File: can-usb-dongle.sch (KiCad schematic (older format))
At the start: 32 parts, among them P1 USB_A, SW1 SW_PUSH, U1 STM32F302C8T, U2 SN65HVD256, U3 MCP1700, U4 SiP32431, X1 8MHz 10ppm

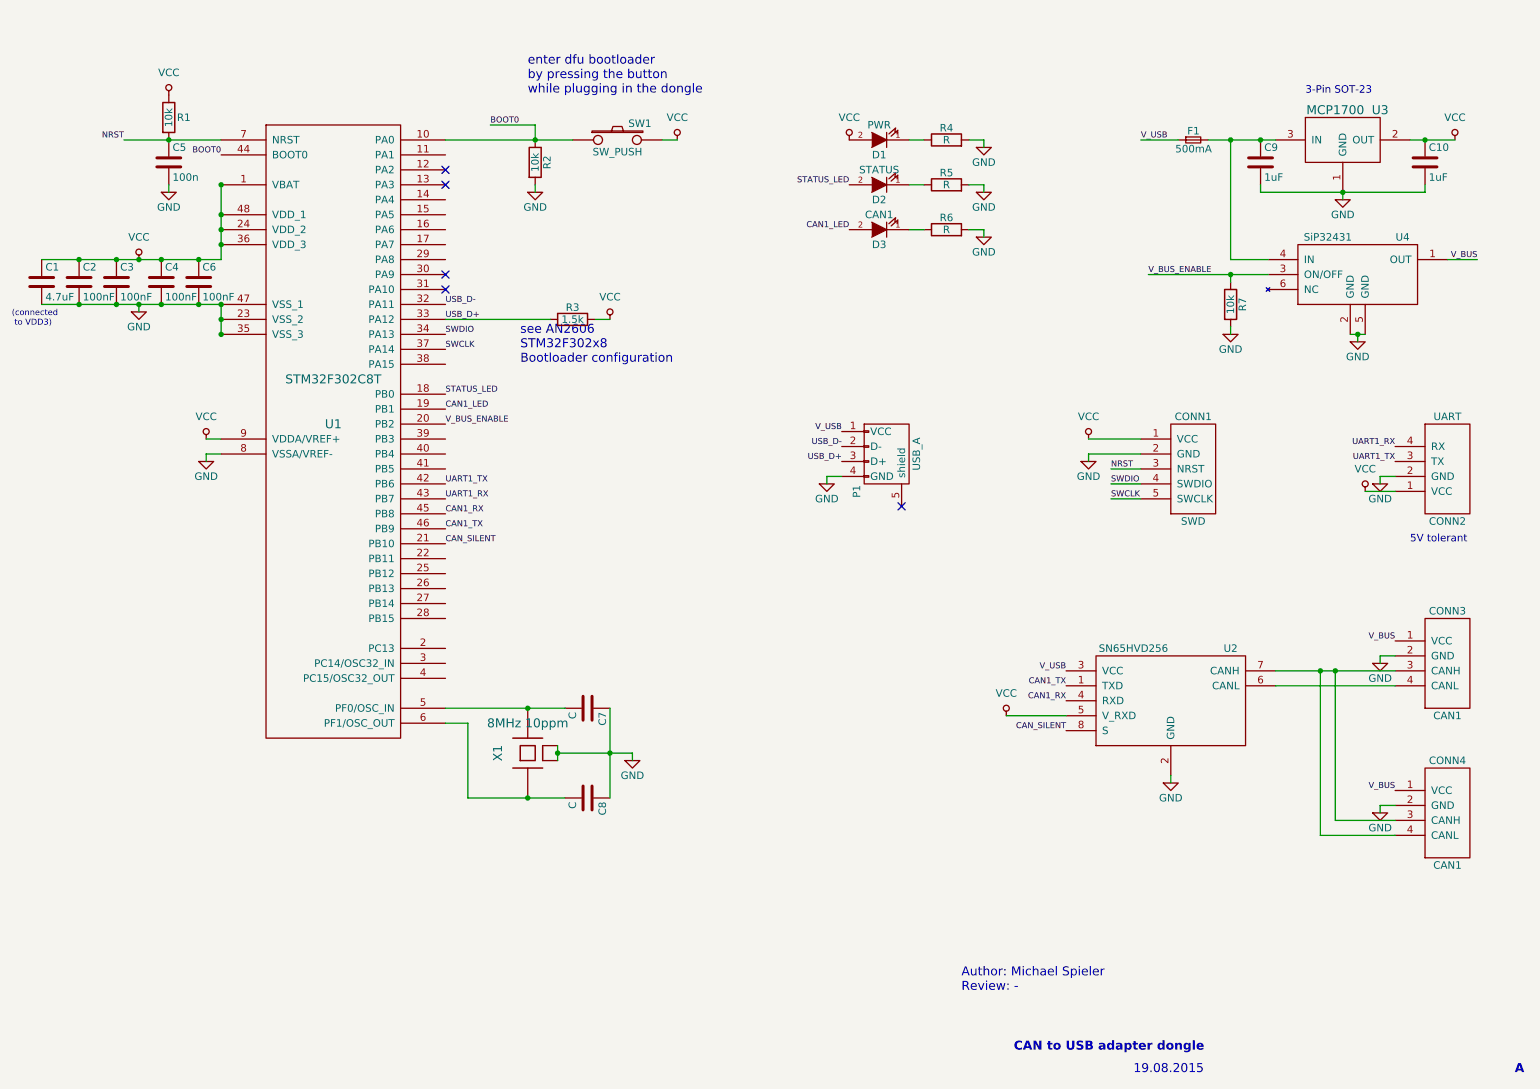
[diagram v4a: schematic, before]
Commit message: Add V_BUS sense and LED, USB pull resistors.
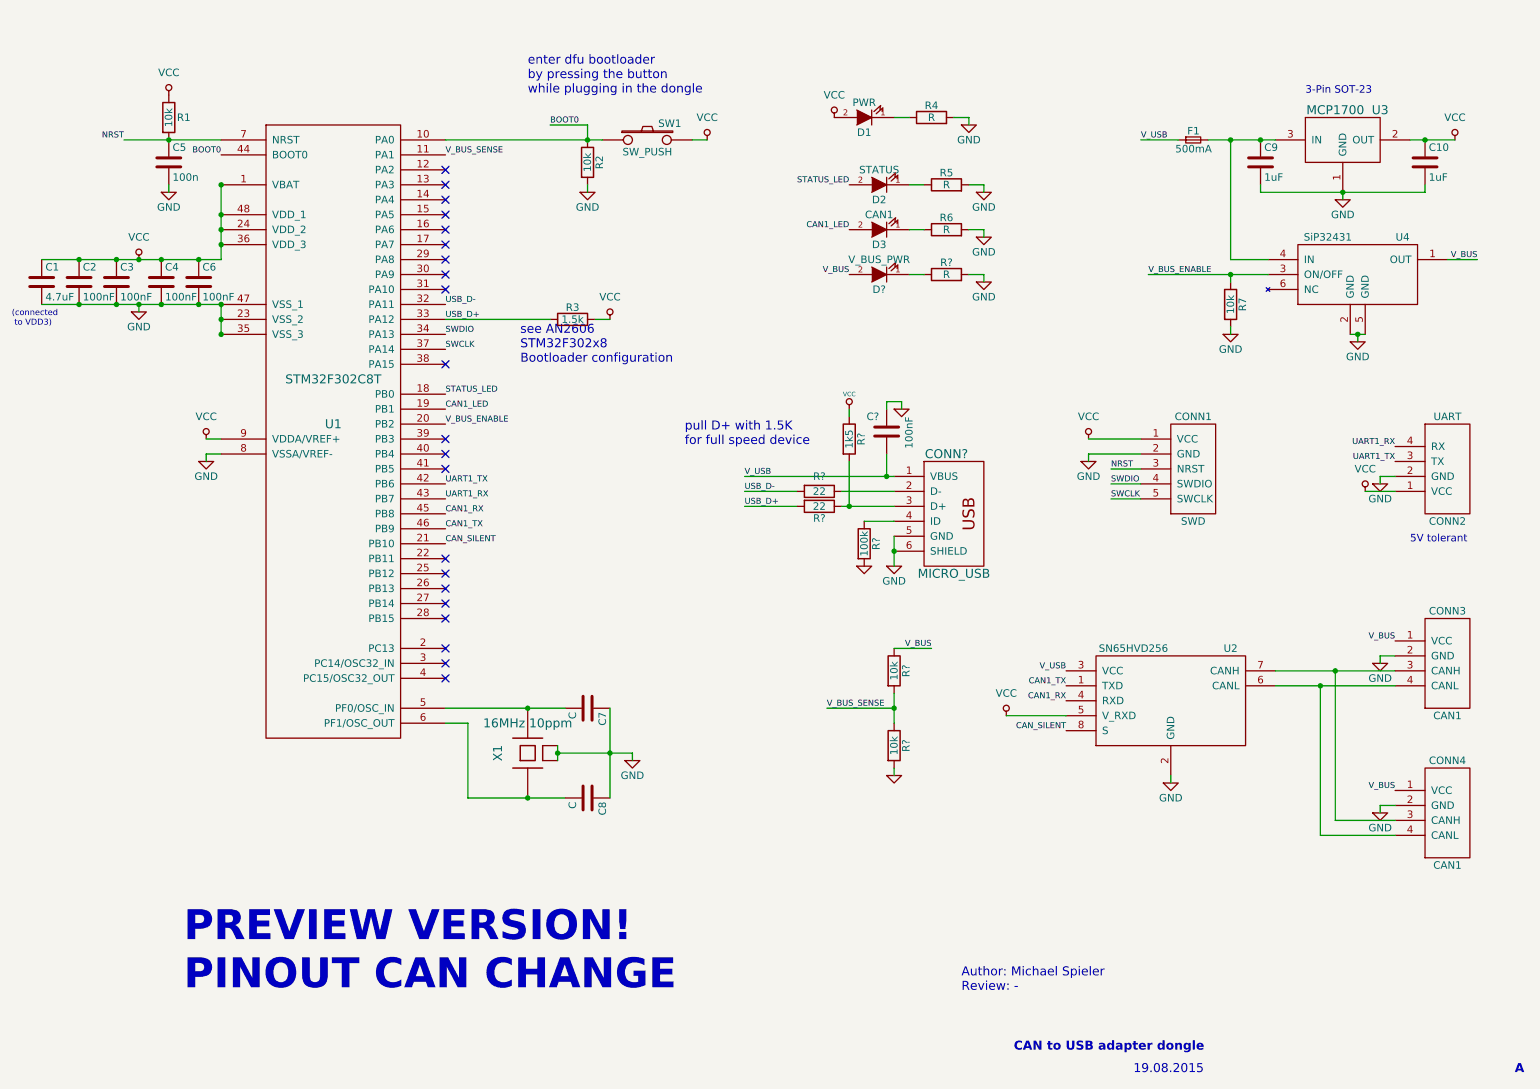
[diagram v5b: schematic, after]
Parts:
- removed P1: USB_A, symbol USB_A
- added C?: 100nF, symbol C
- added CONN?: MICRO_USB, symbol MICRO_USB
- added D?: V_BUS_PWR, LEDs:LED-0603, symbol LED
- added R?: R, Resistors_SMD:R_0603, symbol R
- added R? (x2): 10k, symbol R
- added R? (x2): 22, symbol R
- added R?: 100k, symbol R
- added R?: 1k5, symbol R
- X1: value 8MHz 10ppm -> 16MHz 10ppm
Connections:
- net GND: now also C?.2, CONN?.5 (GND), CONN?.6 (SHIELD), R?.2, R?.2, R?.2
- net USB_D+: now also R?.2
- net USB_D-: now also R?.2
- net VCC: now also R?.1
- net V_BUS: now also D?.2 (A), R?.1
- net V_USB: now also C?.1, CONN?.1 (VBUS)
- net at CONN3.3 (CANH), CONN4.3 (CANH), U2.7 (CANH): no longer CONN4.4 (CANL)
- net at CONN3.4 (CANL), U2.6 (CANL): now also CONN4.4 (CANL)
- net V_BUS_SENSE: now reaches U1.11 (PA1)
- net V_BUS_SENSE: now also R?.1, R?.2
- new net: D?.1 (K), R?.1
- new net: CONN?.2 (D-), R?.1
- new net: CONN?.3 (D+), R?.1, R?.2
- new net: CONN?.4 (ID), R?.1
- no-connect marks 5 -> 21
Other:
- note added: "PREVIEW VERSION!\nPINOUT CAN CHANGE"
- note added: "pull D+ with 1.5K\nfor full speed device"
- moved on the sheet: D1, R2, R4, SW1

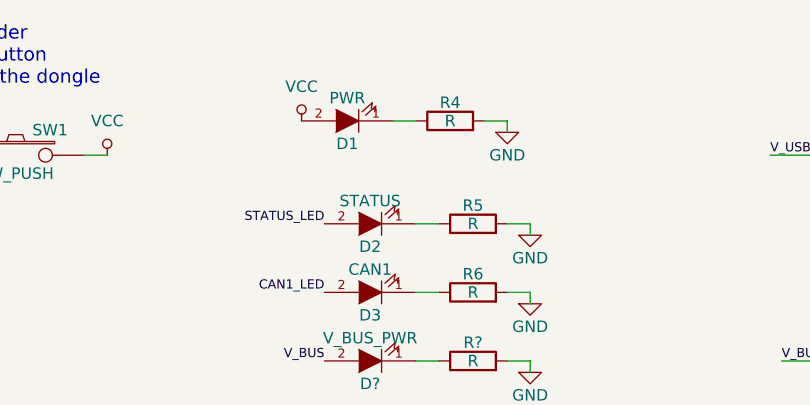
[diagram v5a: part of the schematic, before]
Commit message: Remove PWR LED.
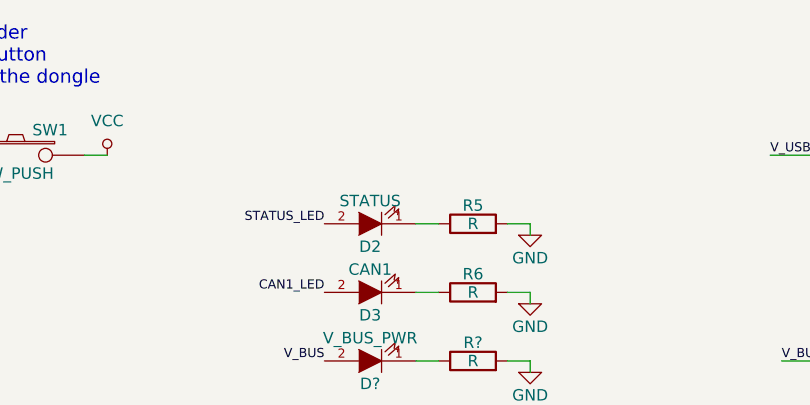
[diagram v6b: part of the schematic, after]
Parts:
- removed D1: PWR, LEDs:LED-0603, symbol LED
- removed R4: R, Resistors_SMD:R_0603, symbol R
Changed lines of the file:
@@
 Text Label 6300 1700 2    40   ~ 0
 STATUS_LED
-$Comp
-L LED D1
-U 1 1 55624F7E
-P 6400 1250
-F 0 "D1" H 6400 1350 50  0000 C CNN
-F 1 "PWR" H 6400 1150 50  0000 C CNN
-F 2 "LEDs:LED-0603" H 6400 1250 60  0001 C CNN
-F 3 "" H 6400 1250 60  0000 C CNN
-	1    6400 1250
-	-1   0    0    1
-$EndComp
-$Comp
-L R R4
-U 1 1 55624F84
-P 6850 1250
-F 0 "R4" V 6930 1250 50  0000 C CNN
-F 1 "R" V 6850 1250 50  0000 C CNN
-F 2 "Resistors_SMD:R_0603" V 6780 1250 30  0001 C CNN
-F 3 "" H 6850 1250 30  0000 C CNN
-	1    6850 1250
-	0    -1   -1   0
-$EndComp
-$Comp
-L GND #PWR015
-U 1 1 55624F8A
-P 7100 1300
-F 0 "#PWR015" H 7100 1050 50  0001 C CNN
-F 1 "GND" H 7100 1200 50  0000 C CNN
-F 2 "" H 7100 1300 60  0000 C CNN
-F 3 "" H 7100 1300 60  0000 C CNN
-	1    7100 1300
-	1    0    0    -1
-$EndComp
-$Comp
-L VCC #PWR016
-U 1 1 55624FD5
-P 6200 1250
-F 0 "#PWR016" H 6200 1100 50  0001 C CNN
-F 1 "VCC" H 6200 1400 50  0000 C CNN
-F 2 "" H 6200 1250 60  0000 C CNN
-F 3 "" H 6200 1250 60  0000 C CNN
-	1    6200 1250
-	1    0    0    -1
-$EndComp
 Text Label 6300 2000 2    40   ~ 0
 CAN1_LED
@@
 	5250 1400 5350 1400
 Wire Wire Line
-	7000 1250 7100 1250
-Wire Wire Line
-	6600 1250 6700 1250
-Wire Wire Line
 	9850 3650 9950 3650
 Wire Wire Line
@@
 	7200 1700 7200 1750
 Wire Wire Line
-	7100 1250 7100 1300
-Wire Wire Line
 	4550 1750 4550 1700

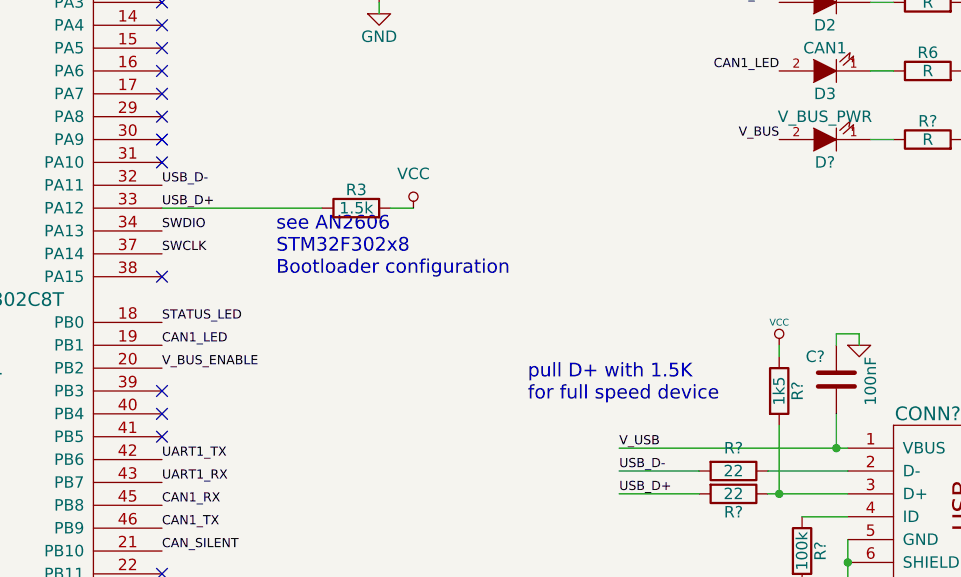
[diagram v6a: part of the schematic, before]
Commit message: Remove duplicate 1.5k USB D+ pullup.
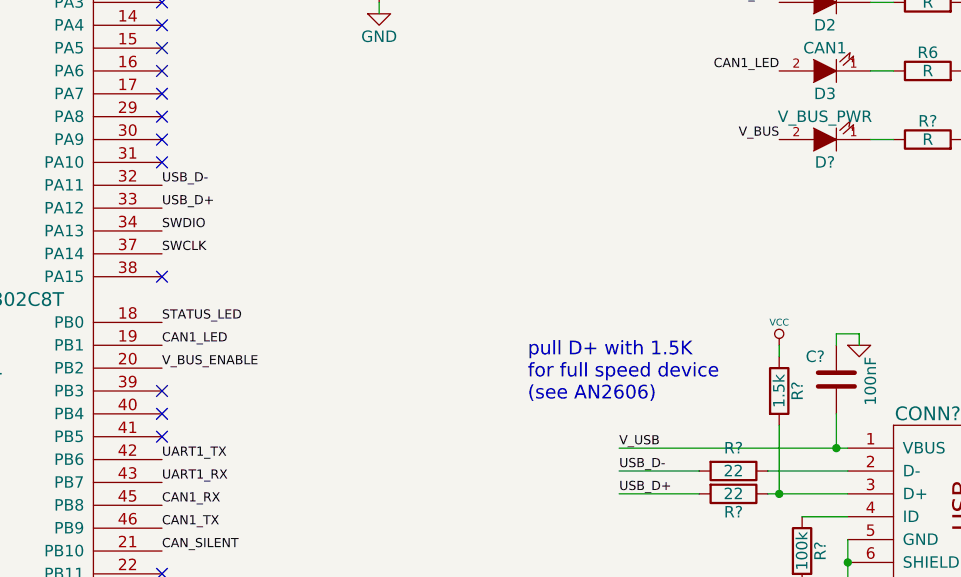
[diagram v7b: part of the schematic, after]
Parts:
- removed R3: 1.5k, Resistors_SMD:R_0603, symbol R
- R?: value 1k5 -> 1.5k
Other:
- note added: "pull D+ with 1.5K\nfor full speed device\n(see AN2606)"
- note removed: "pull D+ with 1.5K\nfor full speed device"
- note removed: "see AN2606\nSTM32F302x8\nBootloader configuration"
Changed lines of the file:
@@
 CAN_SILENT
-$Comp
-L R R3
-U 1 1 5592CBE5
-P 4450 2600
-F 0 "R3" V 4530 2600 50  0000 C CNN
-F 1 "1.5k" V 4450 2600 50  0000 C CNN
-F 2 "Resistors_SMD:R_0603" V 4380 2600 30  0001 C CNN
-F 3 "" H 4450 2600 30  0000 C CNN
-	1    4450 2600
-	0    -1   -1   0
-$EndComp
-$Comp
-L VCC #PWR021
-U 1 1 5592CC45
-P 4700 2600
-F 0 "#PWR021" H 4700 2450 50  0001 C CNN
-F 1 "VCC" H 4700 2750 50  0000 C CNN
-F 2 "" H 4700 2600 60  0000 C CNN
-F 3 "" H 4700 2600 60  0000 C CNN
-	1    4700 2600
-	1    0    0    -1
-$EndComp
-Text Notes 4100 2900 0    60   ~ 0
-see AN2606\nSTM32F302x8\nBootloader configuration
 $Comp
 L GND #PWR022
@@
 	7350 5250 7750 5250
 Wire Wire Line
-	4600 2600 4700 2600
-Wire Wire Line
 	9850 4850 9950 4850
 Wire Wire Line
@@
 Wire Wire Line
 	8850 2650 8850 2700
-Wire Wire Line
-	3600 2600 4300 2600
 Wire Wire Line
 	8850 2350 8850 2300
@@
 P 6300 3400
 F 0 "R?" V 6380 3400 50  0000 C CNN
-F 1 "1k5" V 6300 3400 50  0000 C CNN
+F 1 "1.5k" V 6300 3400 50  0000 C CNN
 F 2 "" V 6230 3400 30  0000 C CNN
 F 3 "" H 6300 3400 30  0000 C CNN
@@
 Connection ~ 6300 3850
 Text Notes 5200 3450 0    60   ~ 0
-pull D+ with 1.5K\nfor full speed device
+pull D+ with 1.5K\nfor full speed device\n(see AN2606)
 Text Notes 1850 7100 0    200  ~ 40
 PREVIEW VERSION!\nPINOUT CAN CHANGE

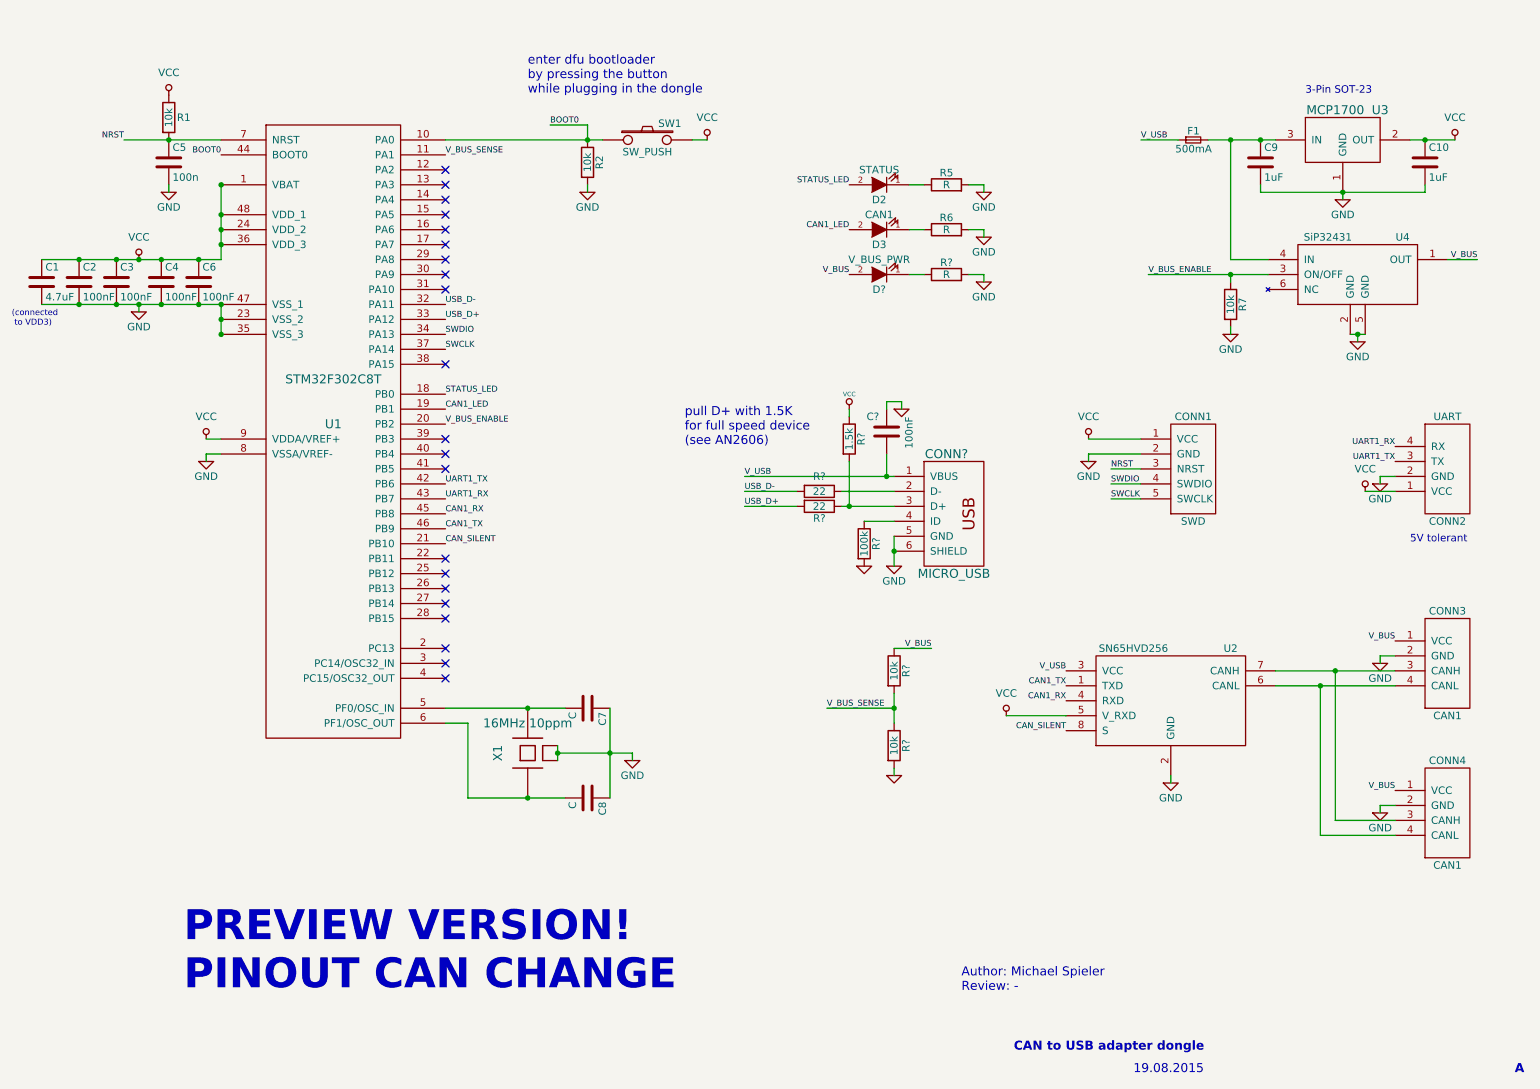
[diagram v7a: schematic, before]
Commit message: USB protection, more capacitors.
- Add NUF2042 ESD proctection for USB
- Correct fuse placement
- Add capacitors to CAN transceiver and SiP32431 switch.
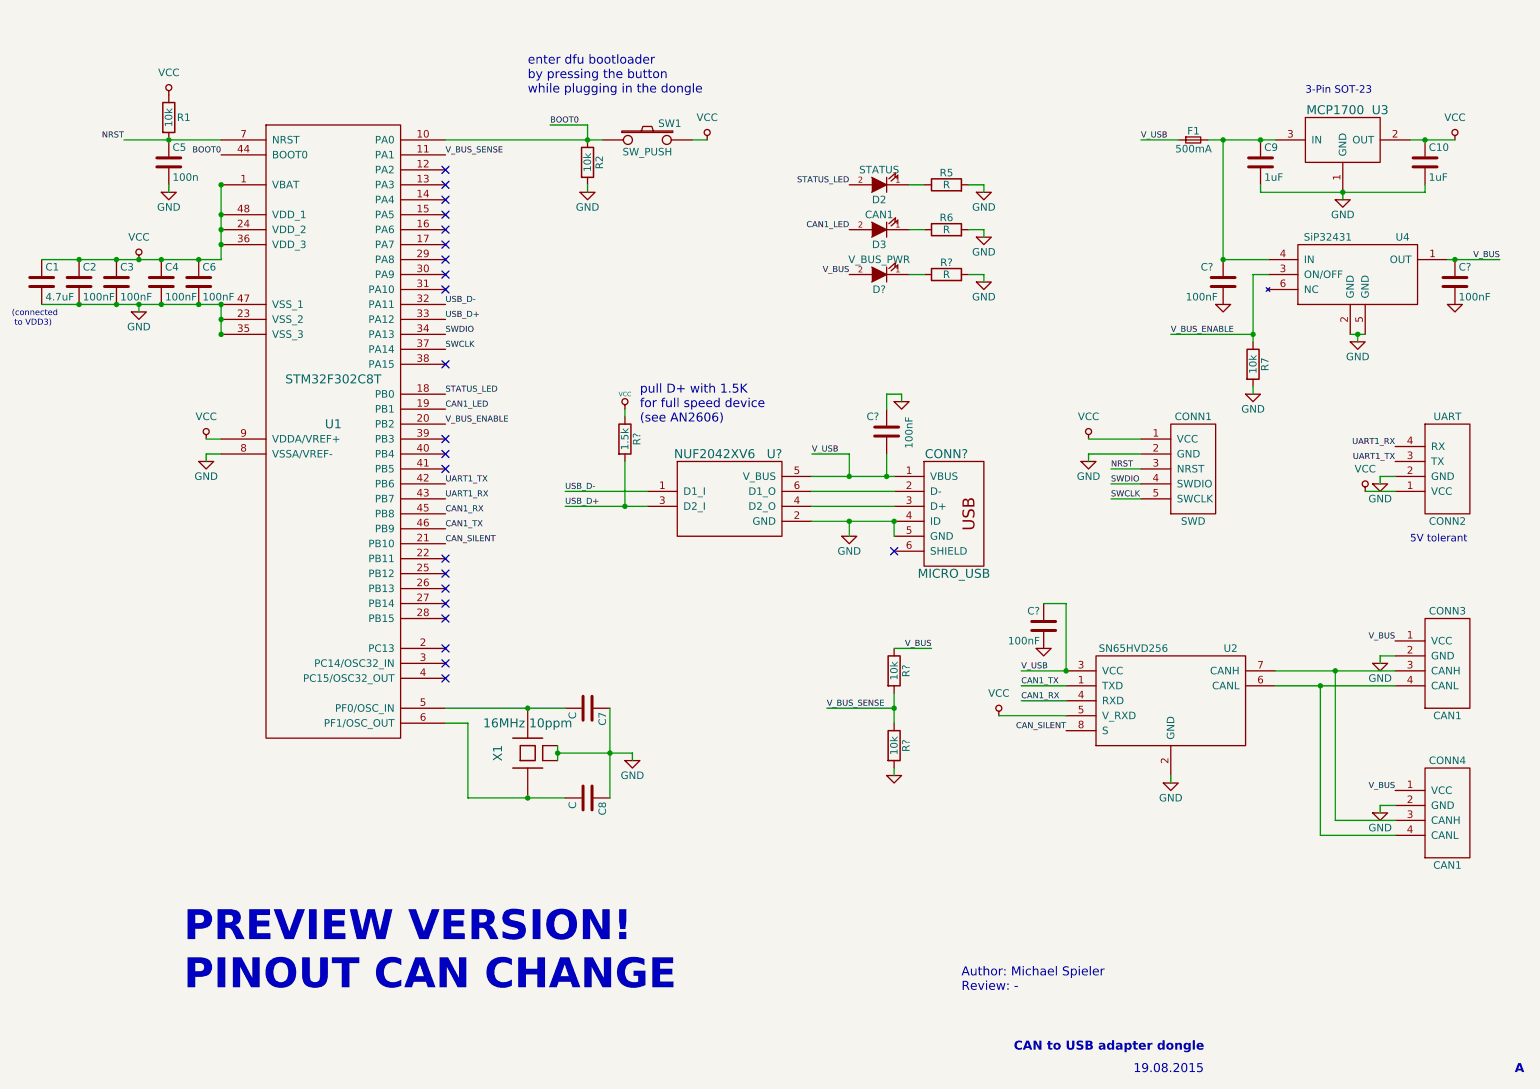
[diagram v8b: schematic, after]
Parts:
- removed R? (x2): 22, symbol R
- removed R?: 100k, symbol R
- added C? (x3): 100nF, symbol C
- added U?: NUF2042XV6, symbol NUF2042XV6
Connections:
- net GND: now also CONN?.4 (ID), C?.2, C?.2, C?.2, U?.2 (GND); no longer CONN?.6 (SHIELD)
- net USB_D+: now also R?.2, U?.3 (D2_I)
- net USB_D-: now also U?.1 (D1_I)
- net V_BUS: now also C?.1
- net V_USB: now also C?.1, U?.5 (V_BUS)
- net at C9.1, F1.2, U3.3 (IN)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: now also C?.1
- net at CONN?.2 (D-): now also U?.6 (D1_O)
- net at CONN?.3 (D+): now also U?.4 (D2_O); no longer R?.2
- no-connect marks 21 -> 22
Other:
- moved on the sheet: R7, R?
